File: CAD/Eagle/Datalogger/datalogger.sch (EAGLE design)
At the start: 12 parts

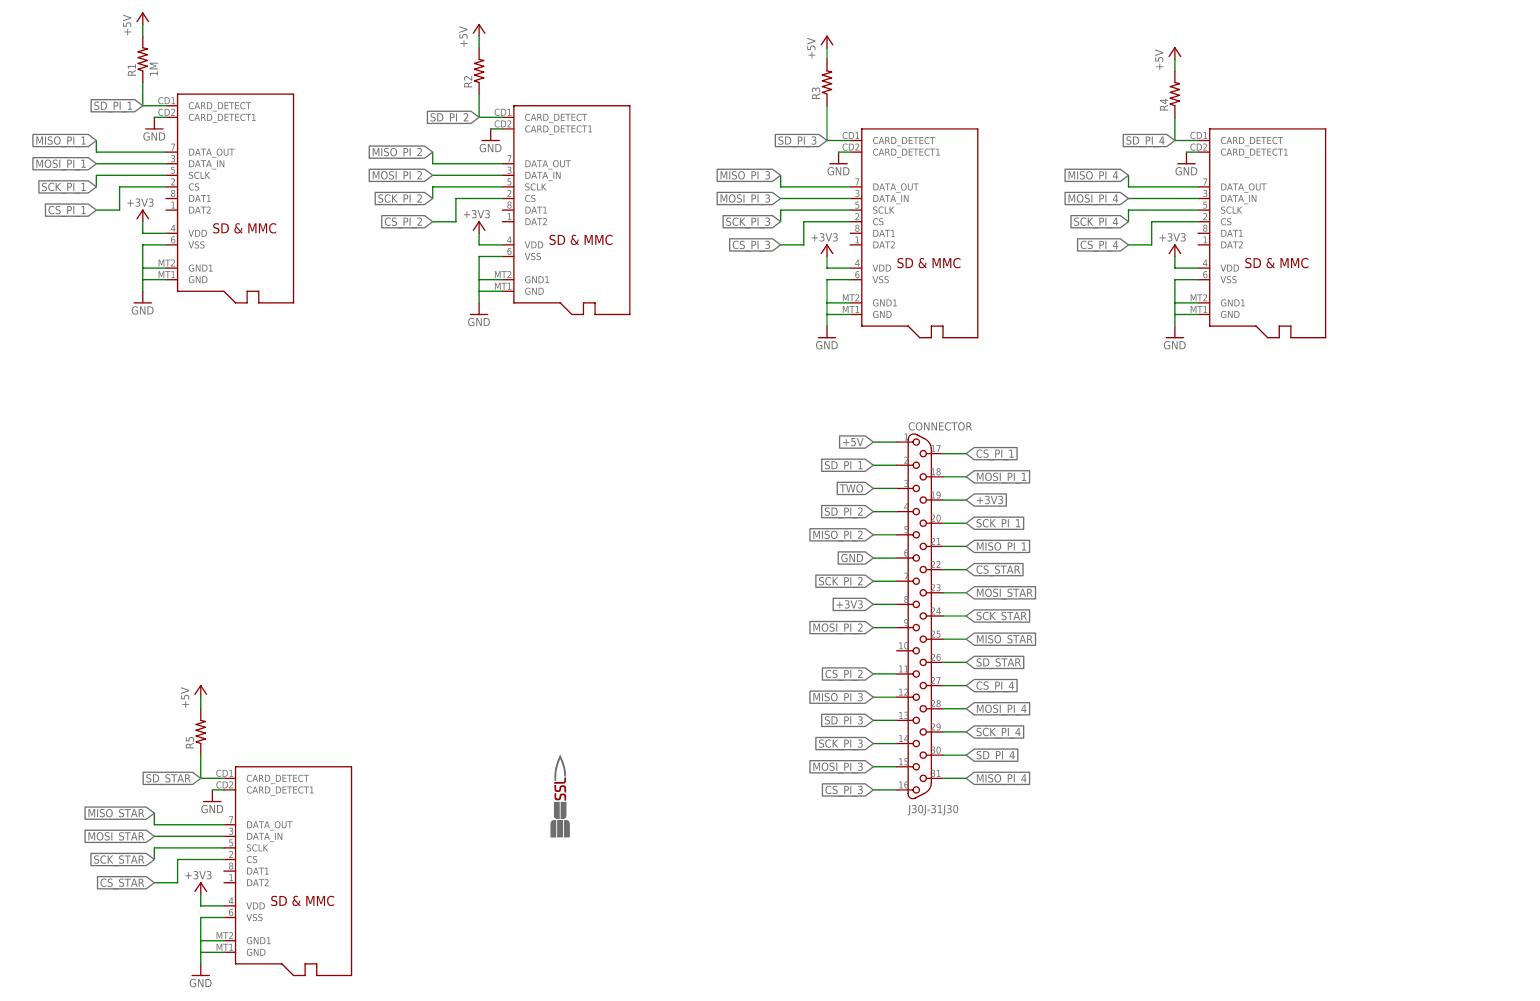
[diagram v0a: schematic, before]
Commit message: Datalogger and STARduino
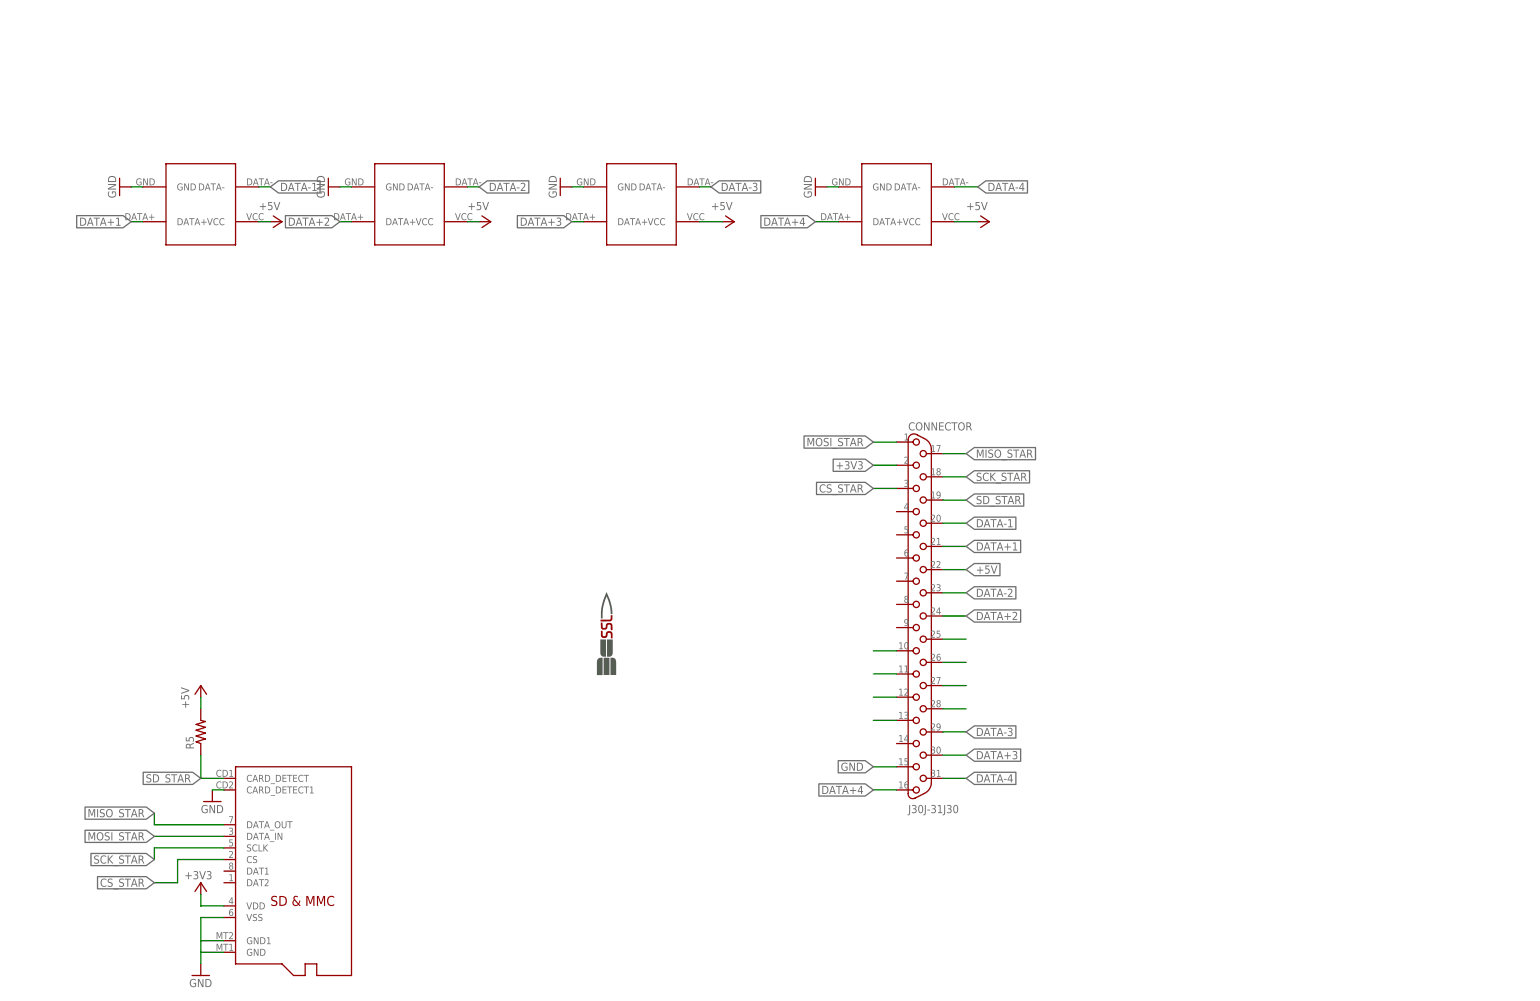
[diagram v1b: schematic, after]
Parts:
- removed R1: 1M, resistor:R-US_R0603
- removed R2, R3, R4: (no value), resistor:R-US_R0603
- PI_1, PI_2, PI_3, PI_4: value MICROSD -> USB_A; device adafruit:MICROSD -> NR_connectors:USB_A
- U$1: value SSL.53IN -> SSL.3IN_SILK; device images:SSL.53IN -> images:SSL.3IN_SILK
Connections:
- removed net CS_PI_1: CONNECTOR.17, PI_1.CS
- removed net CS_PI_2: CONNECTOR.11, PI_2.CS
- removed net CS_PI_3: CONNECTOR.16, PI_3.CS
- removed net CS_PI_4: CONNECTOR.27, PI_4.CS
- removed net MISO_PI_1: CONNECTOR.21, PI_1.DATA_OUT
- removed net MISO_PI_2: CONNECTOR.5, PI_2.DATA_OUT
- removed net MISO_PI_3: CONNECTOR.12, PI_3.DATA_OUT
- removed net MISO_PI_4: CONNECTOR.31, PI_4.DATA_OUT
- removed net MOSI_PI_1: CONNECTOR.18, PI_1.DATA_IN
- removed net MOSI_PI_2: CONNECTOR.9, PI_2.DATA_IN
- removed net MOSI_PI_3: CONNECTOR.15, PI_3.DATA_IN
- removed net MOSI_PI_4: CONNECTOR.28, PI_4.DATA_IN
- removed net SCK_PI_1: CONNECTOR.20, PI_1.SCLK
- removed net SCK_PI_2: CONNECTOR.7, PI_2.SCLK
- removed net SCK_PI_3: CONNECTOR.14, PI_3.SCLK
- removed net SCK_PI_4: CONNECTOR.29, PI_4.SCLK
- removed net SD_PI_1: CONNECTOR.2, PI_1.CARD_DETECT, R1.1
- removed net SD_PI_2: CONNECTOR.4, PI_2.CARD_DETECT, R2.1
- removed net SD_PI_3: CONNECTOR.13, PI_3.CARD_DETECT, R3.1
- removed net SD_PI_4: CONNECTOR.30, PI_4.CARD_DETECT, R4.1
- new net D: CONNECTOR.25
- new net DATA+1: CONNECTOR.21, PI_1.DATA+
- new net DATA+2: CONNECTOR.24, PI_2.DATA+
- new net DATA+3: CONNECTOR.30, PI_3.DATA+
- new net DATA+4: CONNECTOR.16, PI_4.DATA+
- new net DATA-1: CONNECTOR.20, PI_1.DATA-
- new net DATA-2: CONNECTOR.23, PI_2.DATA-
- new net DATA-3: CONNECTOR.29, PI_3.DATA-
- new net DATA-4: CONNECTOR.31, PI_4.DATA-
- new net FOUR: CONNECTOR.11
- new net N$7: CONNECTOR.12
- new net N$8: CONNECTOR.13
- new net ONE: CONNECTOR.27
- new net R: CONNECTOR.26
- new net THREE: CONNECTOR.10
- net +3V3: now also CONNECTOR.2; no longer CONNECTOR.19, CONNECTOR.8, PI_1.VDD, PI_2.VDD, PI_3.VDD, PI_4.VDD
- net +5V: now also CONNECTOR.22, PI_1.VCC, PI_2.VCC, PI_3.VCC, PI_4.VCC; no longer CONNECTOR.1, R1.2, R2.2, R3.2, R4.2
- net CS_STAR: now also CONNECTOR.3; no longer CONNECTOR.22
- net GND: now also CONNECTOR.15; no longer CONNECTOR.6, PI_1.CARD_DETECT1, PI_1.GND1, PI_1.VSS, PI_2.CARD_DETECT1, PI_2.GND1, PI_2.VSS, PI_3.CARD_DETECT1, PI_3.GND1, PI_3.VSS, PI_4.CARD_DETECT1, PI_4.GND1, PI_4.VSS
- net MISO_STAR: now also CONNECTOR.17; no longer CONNECTOR.25
- net MOSI_STAR: now also CONNECTOR.1; no longer CONNECTOR.23
- net SCK_STAR: now also CONNECTOR.18; no longer CONNECTOR.24
- net SD_STAR: now also CONNECTOR.19; no longer CONNECTOR.26
- net TWO: now also CONNECTOR.28; no longer CONNECTOR.3

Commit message: datalogger eagle and NX
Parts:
- removed PI_1, PI_2, PI_3, PI_4: USB_A, NR_connectors:USB_A
- removed R5: (no value), resistor:R-US_R0603
- removed STAR: MICROSD, adafruit:MICROSD
- added C1: 100nF, resistor:C-USC0603
- added R1: 4.7k, resistor:R-US_R0603
- added R2: (no value), resistor:R-US_R0603
- added U$2, U$3: USB_A, NR_connectors:USB_A
- added U1: MT25QL01GBBB8ESF-0AAT, NR_IC:MT25QL01GBBB8ESF-0AAT
- U$1: value SSL.3IN_SILK -> MICRO_SD; device images:SSL.3IN_SILK -> NR_connectors:MICRO_SD
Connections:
- removed net CS_STAR: CONNECTOR.3, STAR.CS
- removed net D: CONNECTOR.25
- removed net FOUR: CONNECTOR.11
- removed net N$7: CONNECTOR.12
- removed net N$8: CONNECTOR.13
- removed net ONE: CONNECTOR.27
- removed net R: CONNECTOR.26
- removed net THREE: CONNECTOR.10
- removed net TWO: CONNECTOR.28
- new net MISO_FLASH: CONNECTOR.1, U1.DQ1
- new net MOSI_FLASH: CONNECTOR.18, U1.DQ0
- new net N$1: R1.2, U1.!RESET!, U1.DQ3/!HOLD!
- new net PB23: CONNECTOR.2, U1.!S!
- new net SCK_FLASH: CONNECTOR.17, U1.C
- net +3V3: now also C1.1, CONNECTOR.21, R1.1, U$1.VDD, U1.VCC; no longer CONNECTOR.2, STAR.VDD
- net +5V: now also CONNECTOR.29, R2.2, U$2.VCC1, U$2.VCC2, U$3.VCC1, U$3.VCC2; no longer CONNECTOR.22, PI_1.VCC, PI_2.VCC, PI_3.VCC, PI_4.VCC, R5.2
- net DATA+1: now also CONNECTOR.23, U$2.DATA+1; no longer CONNECTOR.21, PI_1.DATA+
- net DATA+2: now also CONNECTOR.25, U$2.DATA+2; no longer CONNECTOR.24, PI_2.DATA+
- net DATA+3: now also CONNECTOR.14, U$3.DATA+1; no longer CONNECTOR.30, PI_3.DATA+
- net DATA+4: now also U$3.DATA+2; no longer PI_4.DATA+
- net DATA-1: now also CONNECTOR.22, U$2.DATA-1; no longer CONNECTOR.20, PI_1.DATA-
- net DATA-2: now also CONNECTOR.26, U$2.DATA-2; no longer CONNECTOR.23, PI_2.DATA-
- net DATA-3: now also CONNECTOR.31, U$3.DATA-1; no longer CONNECTOR.29, PI_3.DATA-
- net DATA-4: now also CONNECTOR.30, U$3.DATA-2; no longer CONNECTOR.31, PI_4.DATA-
- net GND: now also C1.2, CONNECTOR.24, U$1.CD1, U$1.G1, U$1.G2, U$1.G3, U$1.G4, U$1.VSS, U$2.GND1, U$2.GND2, U$3.GND1, U$3.GND2, U1.VSS; no longer PI_1.GND, PI_2.GND, PI_3.GND, PI_4.GND, STAR.CARD_DETECT1, STAR.GND, STAR.GND1, STAR.VSS
- net MISO_STAR: now also CONNECTOR.27, U$1.CMD; no longer CONNECTOR.17, STAR.DATA_OUT
- net MOSI_STAR: now also CONNECTOR.19, U$1.DAT0; no longer CONNECTOR.1, STAR.DATA_IN
- net SCK_STAR: now also CONNECTOR.20, U$1.CLK; no longer CONNECTOR.18, STAR.SCLK
- net SD_STAR: now also CONNECTOR.28, R2.1, U$1.CD; no longer CONNECTOR.19, R5.1, STAR.CARD_DETECT
